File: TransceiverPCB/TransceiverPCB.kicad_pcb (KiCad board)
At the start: 2 copper layers, 1 part, among them U1 XC7A35T-1FTG256C

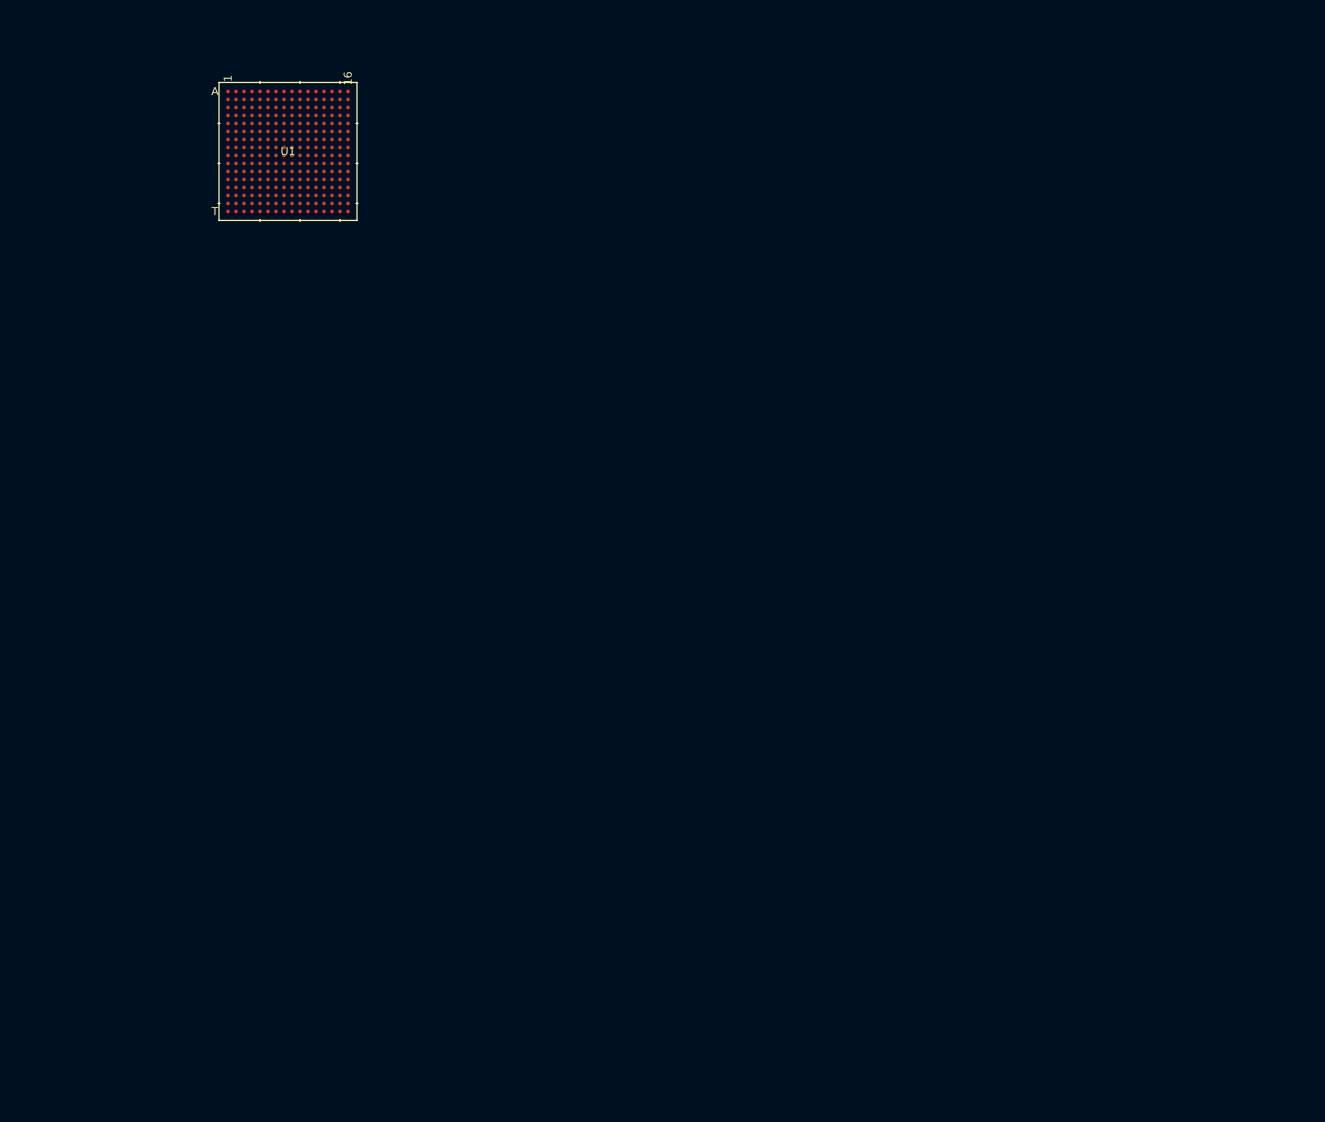
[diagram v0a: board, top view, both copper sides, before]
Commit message: Began PCB
Filled in footprints for components, and began organization of PCB footprints
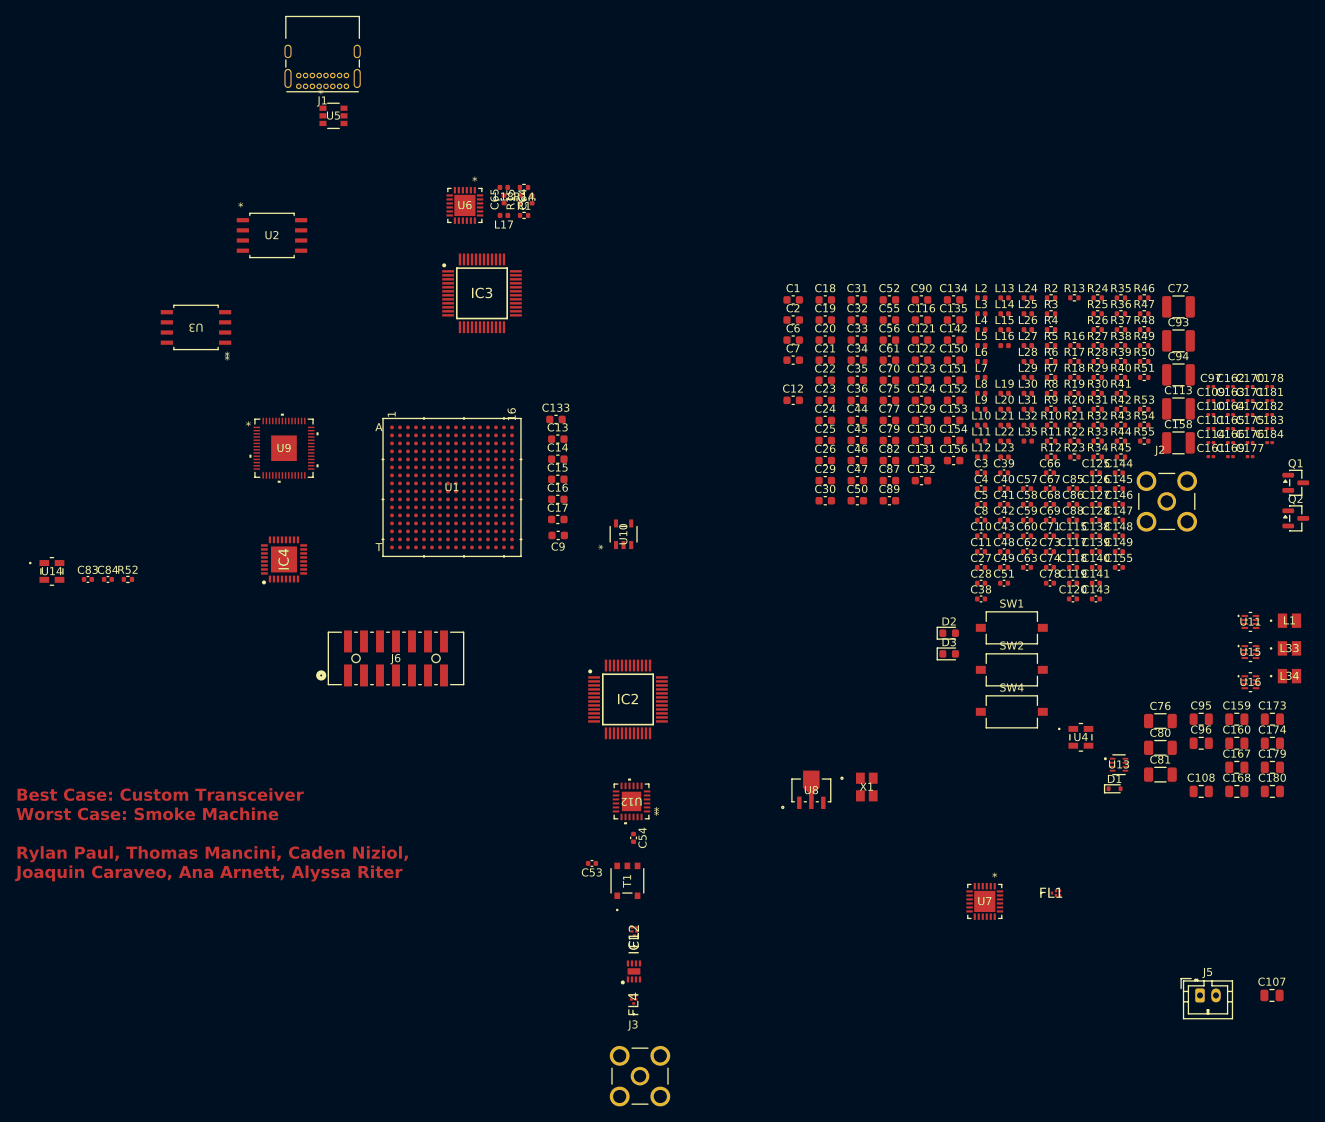
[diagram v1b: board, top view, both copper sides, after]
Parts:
- added C1: 0.1uF, Capacitor_SMD:C_0603_1608Metric, F.Cu at (130.2, 62.6)
- added C10: 22pF, Capacitor_SMD:C_0402_1005Metric, F.Cu at (153.6, 92.1)
- added C107: 4.7uF, Capacitor_SMD:C_0805_2012Metric, F.Cu at (190.0, 149.5)
- added C108: 4.7uF, Capacitor_SMD:C_0805_2012Metric, F.Cu at (181.2, 124.0)
- added C109: 0.47uF, Capacitor_SMD:C_0201_0603Metric, F.Cu at (182.4, 75.2)
- added C11: 22pF, Capacitor_SMD:C_0402_1005Metric, F.Cu at (153.6, 94.0)
- added C110: 0.47uF, Capacitor_SMD:C_0201_0603Metric, F.Cu at (182.4, 76.9)
- added C111: 0.47uF, Capacitor_SMD:C_0201_0603Metric, F.Cu at (182.4, 78.7)
- added C113: 47uF, Capacitor_SMD:C_1210_3225Metric, F.Cu at (178.3, 76.2)
- added C114: 0.47uF, Capacitor_SMD:C_0201_0603Metric, F.Cu at (182.4, 80.4)
- added C115: 120pF, Capacitor_SMD:C_0402_1005Metric, F.Cu at (165.1, 92.1)
- added C116: 0.1uF, Capacitor_SMD:C_0603_1608Metric, F.Cu at (146.2, 65.1)
- added C117: 120pF, Capacitor_SMD:C_0402_1005Metric, F.Cu at (165.1, 94.0)
- added C118: 3.3pF, Capacitor_SMD:C_0402_1005Metric, F.Cu at (165.1, 96.0)
- added C119: 4.7pF, Capacitor_SMD:C_0402_1005Metric, F.Cu at (165.1, 98.0)
- added C12: 10uF, Capacitor_SMD:C_0603_1608Metric, F.Cu at (130.2, 75.1)
- added C120: 3.3pF, Capacitor_SMD:C_0402_1005Metric, F.Cu at (165.1, 99.9)
- added C121: 0.1uF, Capacitor_SMD:C_0603_1608Metric, F.Cu at (146.2, 67.6)
- added C122: 0.1uF, Capacitor_SMD:C_0603_1608Metric, F.Cu at (146.2, 70.1)
- added C123: 0.1uF, Capacitor_SMD:C_0603_1608Metric, F.Cu at (146.2, 72.6)
- added C124: 3.3pF, Capacitor_SMD:C_0603_1608Metric, F.Cu at (146.2, 75.1)
- added C125: 4.7pF, Capacitor_SMD:C_0402_1005Metric, F.Cu at (168.0, 84.2)
- added C126: 3.3pF, Capacitor_SMD:C_0402_1005Metric, F.Cu at (168.0, 86.2)
- added C127: 1nF, Capacitor_SMD:C_0402_1005Metric, F.Cu at (168.0, 88.1)
- added C128: 1nF, Capacitor_SMD:C_0402_1005Metric, F.Cu at (168.0, 90.1)
- added C129: 0.1uF, Capacitor_SMD:C_0603_1608Metric, F.Cu at (146.2, 77.6)
- added C13: 1uF, Capacitor_SMD:C_0603_1608Metric, F.Cu at (100.7, 80.0)
- added C130: 0.1uF, Capacitor_SMD:C_0603_1608Metric, F.Cu at (146.2, 80.1)
- added C131: 0.1uF, Capacitor_SMD:C_0603_1608Metric, F.Cu at (146.2, 82.6)
- added C132: 0.1uF, Capacitor_SMD:C_0603_1608Metric, F.Cu at (146.2, 85.2)
- added C133: 0.1uF, Capacitor_SMD:C_0603_1608Metric, F.Cu at (100.5, 77.5)
- added C134: 0.1uF, Capacitor_SMD:C_0603_1608Metric, F.Cu at (150.2, 62.6)
- added C135: 0.1uF, Capacitor_SMD:C_0603_1608Metric, F.Cu at (150.2, 65.1)
- added C138: 2700pF, Capacitor_SMD:C_0402_1005Metric, F.Cu at (168.0, 92.1)
- added C139: 39nF, Capacitor_SMD:C_0402_1005Metric, F.Cu at (168.0, 94.0)
- added C14: 100nF, Capacitor_SMD:C_0603_1608Metric, F.Cu at (100.7, 82.5)
- added C140: 1200pF, Capacitor_SMD:C_0402_1005Metric, F.Cu at (168.0, 96.0)
- added C141: 120pF, Capacitor_SMD:C_0402_1005Metric, F.Cu at (168.0, 98.0)
- added C142: 0.1uF, Capacitor_SMD:C_0603_1608Metric, F.Cu at (150.2, 67.6)
- added C143: 3.3pF, Capacitor_SMD:C_0402_1005Metric, F.Cu at (168.0, 99.9)
- added C144: 3.3pF, Capacitor_SMD:C_0402_1005Metric, F.Cu at (170.9, 84.2)
- added C145: 120pF, Capacitor_SMD:C_0402_1005Metric, F.Cu at (170.9, 86.2)
- added C146: 4.7pF, Capacitor_SMD:C_0402_1005Metric, F.Cu at (170.9, 88.1)
- added C147: 4.7pF, Capacitor_SMD:C_0402_1005Metric, F.Cu at (170.9, 90.1)
- added C148: 3.3pF, Capacitor_SMD:C_0402_1005Metric, F.Cu at (170.9, 92.1)
- added C149: 3.3pF, Capacitor_SMD:C_0402_1005Metric, F.Cu at (170.9, 94.0)
- added C15: 100nF, Capacitor_SMD:C_0603_1608Metric, F.Cu at (100.7, 85.0)
- added C150: 1nF, Capacitor_SMD:C_0603_1608Metric, F.Cu at (150.2, 70.1)
- added C151: 1nF, Capacitor_SMD:C_0603_1608Metric, F.Cu at (150.2, 72.6)
- added C152: 0.1uF, Capacitor_SMD:C_0603_1608Metric, F.Cu at (150.2, 75.1)
- added C153: .1uF, Capacitor_SMD:C_0603_1608Metric, F.Cu at (150.2, 77.6)
- added C154: .1uF, Capacitor_SMD:C_0603_1608Metric, F.Cu at (150.2, 80.1)
- added C155: 10pF, Capacitor_SMD:C_0402_1005Metric, F.Cu at (170.9, 96.0)
- added C156: 0.1uF, Capacitor_SMD:C_0603_1608Metric, F.Cu at (150.2, 82.6)
- added C158: 47uF, Capacitor_SMD:C_1210_3225Metric, F.Cu at (178.3, 80.4)
- added C159: 4.7uF, Capacitor_SMD:C_0805_2012Metric, F.Cu at (185.6, 115.0)
- added C16: 100nF, Capacitor_SMD:C_0603_1608Metric, F.Cu at (100.7, 87.5)
- added C160: 4.7uF, Capacitor_SMD:C_0805_2012Metric, F.Cu at (185.6, 118.0)
- added C161: 0.47uF, Capacitor_SMD:C_0201_0603Metric, F.Cu at (182.4, 82.2)
- added C162: 0.47uF, Capacitor_SMD:C_0201_0603Metric, F.Cu at (184.8, 73.4)
- added C163: 0.47uF, Capacitor_SMD:C_0201_0603Metric, F.Cu at (184.8, 75.2)
- added C164: 0.47uF, Capacitor_SMD:C_0201_0603Metric, F.Cu at (184.8, 76.9)
- added C165: 0.47uF, Capacitor_SMD:C_0201_0603Metric, F.Cu at (184.8, 78.7)
- added C166: 0.47uF, Capacitor_SMD:C_0201_0603Metric, F.Cu at (184.8, 80.4)
- added C167: 4.7uF, Capacitor_SMD:C_0805_2012Metric, F.Cu at (185.6, 121.0)
- added C168: 4.7uF, Capacitor_SMD:C_0805_2012Metric, F.Cu at (185.6, 124.0)
- added C169: 0.47uF, Capacitor_SMD:C_0201_0603Metric, F.Cu at (184.8, 82.2)
- added C17: 100nF, Capacitor_SMD:C_0603_1608Metric, F.Cu at (100.7, 90.0)
- added C170: 0.47uF, Capacitor_SMD:C_0201_0603Metric, F.Cu at (187.3, 73.4)
- added C171: 0.47uF, Capacitor_SMD:C_0201_0603Metric, F.Cu at (187.3, 75.2)
- added C172: 0.47uF, Capacitor_SMD:C_0201_0603Metric, F.Cu at (187.3, 76.9)
- added C173: 4.7uF, Capacitor_SMD:C_0805_2012Metric, F.Cu at (190.1, 115.0)
- added C174: 4.7uF, Capacitor_SMD:C_0805_2012Metric, F.Cu at (190.1, 118.0)
- added C175: 0.47uF, Capacitor_SMD:C_0201_0603Metric, F.Cu at (187.3, 78.7)
- added C176: 0.47uF, Capacitor_SMD:C_0201_0603Metric, F.Cu at (187.3, 80.4)
- added C177: 0.47uF, Capacitor_SMD:C_0201_0603Metric, F.Cu at (187.3, 82.2)
- added C178: 0.47uF, Capacitor_SMD:C_0201_0603Metric, F.Cu at (189.7, 73.4)
- added C179: 4.7uF, Capacitor_SMD:C_0805_2012Metric, F.Cu at (190.1, 121.0)
- added C18: 100nF, Capacitor_SMD:C_0603_1608Metric, F.Cu at (134.2, 62.6)
- added C180: 4.7uF, Capacitor_SMD:C_0805_2012Metric, F.Cu at (190.1, 124.0)
- added C181: 0.47uF, Capacitor_SMD:C_0201_0603Metric, F.Cu at (189.7, 75.2)
- added C182: 0.47uF, Capacitor_SMD:C_0201_0603Metric, F.Cu at (189.7, 76.9)
- added C183: 0.47uF, Capacitor_SMD:C_0201_0603Metric, F.Cu at (189.7, 78.7)
- added C184: 0.47uF, Capacitor_SMD:C_0201_0603Metric, F.Cu at (189.7, 80.4)
- added C19: 100nF, Capacitor_SMD:C_0603_1608Metric, F.Cu at (134.2, 65.1)
- added C2: 0.1uF, Capacitor_SMD:C_0603_1608Metric, F.Cu at (130.2, 65.1)
- added C20: 100nF, Capacitor_SMD:C_0603_1608Metric, F.Cu at (134.2, 67.6)
- added C21: 1uF, Capacitor_SMD:C_0603_1608Metric, F.Cu at (134.2, 70.1)
- added C22: 100nF, Capacitor_SMD:C_0603_1608Metric, F.Cu at (134.2, 72.6)
- added C23: 100nF, Capacitor_SMD:C_0603_1608Metric, F.Cu at (134.2, 75.1)
- added C24: 1uF, Capacitor_SMD:C_0603_1608Metric, F.Cu at (134.2, 77.6)
- added C25: 1uF, Capacitor_SMD:C_0603_1608Metric, F.Cu at (134.2, 80.1)
- added C26: 0.1uF, Capacitor_SMD:C_0603_1608Metric, F.Cu at (134.2, 82.6)
- added C27: 4.7uF, Capacitor_SMD:C_0402_1005Metric, F.Cu at (153.6, 96.0)
- added C28: 0.1uF, Capacitor_SMD:C_0402_1005Metric, F.Cu at (153.6, 98.0)
- added C29: 10uF, Capacitor_SMD:C_0603_1608Metric, F.Cu at (134.2, 85.2)
- added C3: 22nF, Capacitor_SMD:C_0402_1005Metric, F.Cu at (153.6, 84.2)
- added C30: 100nF, Capacitor_SMD:C_0603_1608Metric, F.Cu at (134.2, 87.7)
- added C31: 10uF, Capacitor_SMD:C_0603_1608Metric, F.Cu at (138.2, 62.6)
- added C32: 10uF, Capacitor_SMD:C_0603_1608Metric, F.Cu at (138.2, 65.1)
- added C33: 10uF, Capacitor_SMD:C_0603_1608Metric, F.Cu at (138.2, 67.6)
- added C34: 10uF, Capacitor_SMD:C_0603_1608Metric, F.Cu at (138.2, 70.1)
- added C35: 100nF, Capacitor_SMD:C_0603_1608Metric, F.Cu at (138.2, 72.6)
- added C36: 1uF, Capacitor_SMD:C_0603_1608Metric, F.Cu at (138.2, 75.1)
- added C38: 270pF, Capacitor_SMD:C_0402_1005Metric, F.Cu at (153.6, 99.9)
- added C39: 270pF, Capacitor_SMD:C_0402_1005Metric, F.Cu at (156.5, 84.2)
- added C4: 22nF, Capacitor_SMD:C_0402_1005Metric, F.Cu at (153.6, 86.2)
- added C40: 91pF, Capacitor_SMD:C_0402_1005Metric, F.Cu at (156.5, 86.2)
- added C41: 91pF, Capacitor_SMD:C_0402_1005Metric, F.Cu at (156.5, 88.1)
- added C42: 68pF, Capacitor_SMD:C_0402_1005Metric, F.Cu at (156.5, 90.1)
- added C43: 68pF, Capacitor_SMD:C_0402_1005Metric, F.Cu at (156.5, 92.1)
- added C44: 1uF, Capacitor_SMD:C_0603_1608Metric, F.Cu at (138.2, 77.6)
- added C45: 1uF, Capacitor_SMD:C_0603_1608Metric, F.Cu at (138.2, 80.1)
- added C46: .1uF, Capacitor_SMD:C_0603_1608Metric, F.Cu at (138.2, 82.6)
- added C47: .1uF, Capacitor_SMD:C_0603_1608Metric, F.Cu at (138.2, 85.2)
- added C48: 100pF, Capacitor_SMD:C_0402_1005Metric, F.Cu at (156.5, 94.0)
- added C49: 100pF, Capacitor_SMD:C_0402_1005Metric, F.Cu at (156.5, 96.0)
- added C5: 100pF, Capacitor_SMD:C_0402_1005Metric, F.Cu at (153.6, 88.1)
- added C50: .1uF, Capacitor_SMD:C_0603_1608Metric, F.Cu at (138.2, 87.7)
- added C51: 100pF, Capacitor_SMD:C_0402_1005Metric, F.Cu at (156.5, 98.0)
- added C52: .1uF, Capacitor_SMD:C_0603_1608Metric, F.Cu at (142.2, 62.6)
- added C53: 1000pF, Capacitor_SMD:C_0402_1005Metric, F.Cu at (105.0, 133.0)
- added C54: 1000pF, Capacitor_SMD:C_0402_1005Metric, F.Cu at (110.2, 129.8)
- added C55: 1uF, Capacitor_SMD:C_0603_1608Metric, F.Cu at (142.2, 65.1)
- added C56: 1uF, Capacitor_SMD:C_0603_1608Metric, F.Cu at (142.2, 67.6)
- added C57: 47pF, Capacitor_SMD:C_0402_1005Metric, F.Cu at (159.4, 86.2)
- added C58: 6.8pF, Capacitor_SMD:C_0402_1005Metric, F.Cu at (159.4, 88.1)
- added C59: 100pF, Capacitor_SMD:C_0402_1005Metric, F.Cu at (159.4, 90.1)
- added C6: 0.1uF, Capacitor_SMD:C_0603_1608Metric, F.Cu at (130.2, 67.6)
- added C60: 10nF, Capacitor_SMD:C_0402_1005Metric, F.Cu at (159.4, 92.1)
- added C61: 10uF, Capacitor_SMD:C_0603_1608Metric, F.Cu at (142.2, 70.1)
- added C62: 47pF, Capacitor_SMD:C_0402_1005Metric, F.Cu at (159.4, 94.0)
- added C63: 2.2pF, Capacitor_SMD:C_0402_1005Metric, F.Cu at (159.4, 96.0)
- added C64: 53.62pF, Capacitor_SMD:C_0402_1005Metric, F.Cu at (97.5, 50.0)
- added C65: 350.1pF, Capacitor_SMD:C_0402_1005Metric, F.Cu at (94.0, 50.0)
- added C66: 53.62pF, Capacitor_SMD:C_0402_1005Metric, F.Cu at (162.2, 84.2)
- added C67: 350.1pF, Capacitor_SMD:C_0402_1005Metric, F.Cu at (162.2, 86.2)
- added C68: 10uF, Capacitor_SMD:C_0402_1005Metric, F.Cu at (162.2, 88.1)
- added C69: 4.7uF, Capacitor_SMD:C_0402_1005Metric, F.Cu at (162.2, 90.1)
- added C7: 0.1uF, Capacitor_SMD:C_0603_1608Metric, F.Cu at (130.2, 70.1)
- added C70: 100nF, Capacitor_SMD:C_0603_1608Metric, F.Cu at (142.2, 72.6)
- added C71: 10uF, Capacitor_SMD:C_0402_1005Metric, F.Cu at (162.2, 92.1)
- added C72: 47uF, Capacitor_SMD:C_1210_3225Metric, F.Cu at (178.3, 63.4)
- added C73: 4.7uF, Capacitor_SMD:C_0402_1005Metric, F.Cu at (162.2, 94.0)
- added C74: 10uF, Capacitor_SMD:C_0402_1005Metric, F.Cu at (162.2, 96.0)
- added C75: 0.1uF, Capacitor_SMD:C_0603_1608Metric, F.Cu at (142.2, 75.1)
- added C76: 47uF, Capacitor_SMD:C_1206_3216Metric, F.Cu at (176.1, 115.2)
- added C77: 0.1uF, Capacitor_SMD:C_0603_1608Metric, F.Cu at (142.2, 77.6)
- added C78: 6.8nF, Capacitor_SMD:C_0402_1005Metric, F.Cu at (162.2, 98.0)
- added C79: 100nF, Capacitor_SMD:C_0603_1608Metric, F.Cu at (142.2, 80.1)
- added C8: 100pF, Capacitor_SMD:C_0402_1005Metric, F.Cu at (153.6, 90.1)
- added C80: 22uF, Capacitor_SMD:C_1206_3216Metric, F.Cu at (176.1, 118.5)
- added C81: 22uF, Capacitor_SMD:C_1206_3216Metric, F.Cu at (176.1, 121.9)
- added C82: 0.1uF, Capacitor_SMD:C_0603_1608Metric, F.Cu at (142.2, 82.6)
- added C83: 1nF, Capacitor_SMD:C_0402_1005Metric, F.Cu at (42.0, 97.5)
- added C84: 1nF, Capacitor_SMD:C_0402_1005Metric, F.Cu at (44.5, 97.5)
- added C85: 22pF, Capacitor_SMD:C_0402_1005Metric, F.Cu at (165.1, 86.2)
- added C86: 10pF, Capacitor_SMD:C_0402_1005Metric, F.Cu at (165.1, 88.1)
- added C87: 0.1uF, Capacitor_SMD:C_0603_1608Metric, F.Cu at (142.2, 85.2)
- added C88: 10pF, Capacitor_SMD:C_0402_1005Metric, F.Cu at (165.1, 90.1)
- added C89: 0.1uF, Capacitor_SMD:C_0603_1608Metric, F.Cu at (142.2, 87.7)
- added C9: 100nF, Capacitor_SMD:C_0603_1608Metric, F.Cu at (100.8, 92.0)
- added C90: 1uF, Capacitor_SMD:C_0603_1608Metric, F.Cu at (146.2, 62.6)
- added C93: 100uF, Capacitor_SMD:C_1210_3225Metric, F.Cu at (178.3, 67.7)
- added C94: 100uF, Capacitor_SMD:C_1210_3225Metric, F.Cu at (178.3, 71.9)
- added C95: 4.7uF, Capacitor_SMD:C_0805_2012Metric, F.Cu at (181.2, 115.0)
- added C96: 4.7uF, Capacitor_SMD:C_0805_2012Metric, F.Cu at (181.2, 118.0)
- added C97: 0.47uF, Capacitor_SMD:C_0201_0603Metric, F.Cu at (182.4, 73.4)
- added D1: ESD5Z5V0, LIB_IRISHSAT:P38_SOD-523, F.Cu at (169.6, 123.7)
- added D2: LED, LED_SMD:LED_0603_1608Metric, F.Cu at (149.6, 104.2)
- added D3: LED, LED_SMD:LED_0603_1608Metric, F.Cu at (149.6, 106.8)
- added FL1: B39921B2672P810, LIB_IRISHSAT:B39921B2672P810, F.Cu at (163.0, 136.7)
- added FL2: B39921B2672P810, LIB_IRISHSAT:B39921B2672P810, F.Cu at (110.3, 141.5)
- added FL4: B39921B2672P810, LIB_IRISHSAT:B39921B2672P810, F.Cu at (110.2, 150.0)
- added IC1: QPL6220QTR7, LIB_IRISHSAT:SON50P200X200X90-9N-D, F.Cu at (110.2, 146.5)
- added IC2: AD9218BSTZ-65, LIB_IRISHSAT:QFP50P900X900X160-48N, F.Cu at (109.5, 112.5)
- added IC3: AD9763ASTZ, LIB_IRISHSAT:QFP50P900X900X160-48N, F.Cu at (91.2, 61.7)
- added IC4: ADF4351BCPZ-RL7, LIB_IRISHSAT:QFN50P500X500X80-33N-D, F.Cu at (66.5, 95.0)
- added J1: USB4085-GF-A_REVB, Connector_USB:USB_C_Receptacle_GCT_USB4085, F.Cu at (74.3, 35.9)
- added J2: RFPC-SMA27-F, LIB_IRISHSAT:GRADCONN_RFPC-SMA27-F, F.Cu at (176.8, 87.8)
- added J3: RFPC-SMA27-F, LIB_IRISHSAT:GRADCONN_RFPC-SMA27-F, F.Cu at (111.0, 159.6)
- added J5: Conn_01x02, Connector_JST:JST_PH_B2B-PH-K_1x02_P2.00mm_Vertical, F.Cu at (181.0, 149.5)
- added J6: 878321420, LIB_IRISHSAT:CONN14_878321420_MOL, F.Cu at (80.5, 107.4)
- added L1: 2.2uH, LIB_IRISHSAT:IND_DFE2016_MUR, F.Cu at (192.2, 102.7)
- added L10: 27uH, Inductor_SMD:L_0402_1005Metric, F.Cu at (153.7, 78.2)
- added L11: 10uH, Inductor_SMD:L_0402_1005Metric, F.Cu at (153.7, 80.2)
- added L12: 10uH, Inductor_SMD:L_0402_1005Metric, F.Cu at (153.7, 82.2)
- added L13: 27uH, Inductor_SMD:L_0402_1005Metric, F.Cu at (156.6, 62.3)
- added L14: 10uH, Inductor_SMD:L_0402_1005Metric, F.Cu at (156.6, 64.3)
- added L15: 10uH, Inductor_SMD:L_0402_1005Metric, F.Cu at (156.6, 66.3)
- added L16: 47nH, Inductor_SMD:L_0402_1005Metric, F.Cu at (156.6, 68.3)
- added L17: 771.1nH, Inductor_SMD:L_0402_1005Metric, F.Cu at (94.0, 52.0)
- added L18: 771.1nH, Inductor_SMD:L_0402_1005Metric, F.Cu at (94.0, 48.5)
- added L19: 771.1nH, Inductor_SMD:L_0402_1005Metric, F.Cu at (156.6, 74.2)
- added L2: 120nH, Inductor_SMD:L_0402_1005Metric, F.Cu at (153.7, 62.3)
- added L20: 771.1nH, Inductor_SMD:L_0402_1005Metric, F.Cu at (156.6, 76.2)
- added L21: 2.7nH, Inductor_SMD:L_0402_1005Metric, F.Cu at (156.6, 78.2)
- added L22: 2.7nH, Inductor_SMD:L_0402_1005Metric, F.Cu at (156.6, 80.2)
- added L23: 2.7nH, Inductor_SMD:L_0402_1005Metric, F.Cu at (156.6, 82.2)
- added L24: 2.7nH, Inductor_SMD:L_0402_1005Metric, F.Cu at (159.5, 62.3)
- added L25: 19nH, Inductor_SMD:L_0402_1005Metric, F.Cu at (159.5, 64.3)
- added L26: 19nH, Inductor_SMD:L_0402_1005Metric, F.Cu at (159.5, 66.3)
- added L27: 19nH, Inductor_SMD:L_0402_1005Metric, F.Cu at (159.5, 68.3)
- added L28: 19nH, Inductor_SMD:L_0402_1005Metric, F.Cu at (159.5, 70.3)
- added L29: 2.7nH, Inductor_SMD:L_0402_1005Metric, F.Cu at (159.5, 72.2)
- added L3: 120nH, Inductor_SMD:L_0402_1005Metric, F.Cu at (153.7, 64.3)
- added L30: 2.7nH, Inductor_SMD:L_0402_1005Metric, F.Cu at (159.5, 74.2)
- added L31: 2.7nH, Inductor_SMD:L_0402_1005Metric, F.Cu at (159.5, 76.2)
- added L32: 2.7nH, Inductor_SMD:L_0402_1005Metric, F.Cu at (159.5, 78.2)
- added L33: 2.2uH, LIB_IRISHSAT:IND_DFE2016_MUR, F.Cu at (192.2, 106.1)
- added L34: 2.2uH, LIB_IRISHSAT:IND_DFE2016_MUR, F.Cu at (192.2, 109.6)
- added L35: 2.7uH, Inductor_SMD:L_0402_1005Metric, F.Cu at (159.5, 80.2)
- added L4: 27uH, Inductor_SMD:L_0402_1005Metric, F.Cu at (153.7, 66.3)
- added L5: 27uH, Inductor_SMD:L_0402_1005Metric, F.Cu at (153.7, 68.3)
- added L6: 27uH, Inductor_SMD:L_0402_1005Metric, F.Cu at (153.7, 70.3)
- added L7: 27uH, Inductor_SMD:L_0402_1005Metric, F.Cu at (153.7, 72.2)
- added L8: 27uH, Inductor_SMD:L_0402_1005Metric, F.Cu at (153.7, 74.2)
- added L9: 27uH, Inductor_SMD:L_0402_1005Metric, F.Cu at (153.7, 76.2)
- added Q1: AO3401A, Package_TO_SOT_SMD:SOT-23, F.Cu at (193.0, 85.4)
- added Q2: AO3401A, Package_TO_SOT_SMD:SOT-23, F.Cu at (193.0, 89.9)
- added R1: 50, Resistor_SMD:R_0402_1005Metric, F.Cu at (96.5, 52.0)
- added R10: 10k, Resistor_SMD:R_0402_1005Metric, F.Cu at (162.4, 78.2)
- added R11: 500, Resistor_SMD:R_0402_1005Metric, F.Cu at (162.4, 80.2)
- added R12: 500, Resistor_SMD:R_0402_1005Metric, F.Cu at (162.4, 82.2)
- added R13: 1k, Resistor_SMD:R_0402_1005Metric, F.Cu at (165.3, 62.3)
- added R14: 50, Resistor_SMD:R_0402_1005Metric, F.Cu at (96.5, 48.5)
- added R15: 100, Resistor_SMD:R_0402_1005Metric, F.Cu at (96.0, 50.0)
- added R16: 50, Resistor_SMD:R_0402_1005Metric, F.Cu at (165.3, 68.3)
- added R17: 50, Resistor_SMD:R_0402_1005Metric, F.Cu at (165.3, 70.3)
- added R18: 100, Resistor_SMD:R_0402_1005Metric, F.Cu at (165.3, 72.2)
- added R19: 10k, Resistor_SMD:R_0402_1005Metric, F.Cu at (165.3, 74.2)
- added R2: DNF, Resistor_SMD:R_0402_1005Metric, F.Cu at (162.4, 62.3)
- added R20: 1k, Resistor_SMD:R_0402_1005Metric, F.Cu at (165.3, 76.2)
- added R21: 1k, Resistor_SMD:R_0402_1005Metric, F.Cu at (165.3, 78.2)
- added R22: 1k, Resistor_SMD:R_0402_1005Metric, F.Cu at (165.3, 80.2)
- added R23: 1k, Resistor_SMD:R_0402_1005Metric, F.Cu at (165.3, 82.2)
- added R24: 1k, Resistor_SMD:R_0402_1005Metric, F.Cu at (168.2, 62.3)
- added R25: 1k, Resistor_SMD:R_0402_1005Metric, F.Cu at (168.2, 64.3)
- added R26: 1k, Resistor_SMD:R_0402_1005Metric, F.Cu at (168.2, 66.3)
- added R27: 10k, Resistor_SMD:R_0402_1005Metric, F.Cu at (168.2, 68.3)
- added R28: 10k, Resistor_SMD:R_0402_1005Metric, F.Cu at (168.2, 70.3)
- added R29: 1k, Resistor_SMD:R_0402_1005Metric, F.Cu at (168.2, 72.2)
- added R3: 1k, Resistor_SMD:R_0402_1005Metric, F.Cu at (162.4, 64.3)
- added R30: DNF, Resistor_SMD:R_0402_1005Metric, F.Cu at (168.2, 74.2)
- added R31: 470k, Resistor_SMD:R_0402_1005Metric, F.Cu at (168.2, 76.2)
- added R32: 54k, Resistor_SMD:R_0402_1005Metric, F.Cu at (168.2, 78.2)
- added R33: 100, Resistor_SMD:R_0402_1005Metric, F.Cu at (168.2, 80.2)
- added R34: 10k, Resistor_SMD:R_0402_1005Metric, F.Cu at (168.2, 82.2)
- added R35: 360, Resistor_SMD:R_0402_1005Metric, F.Cu at (171.1, 62.3)
- added R36: 680, Resistor_SMD:R_0402_1005Metric, F.Cu at (171.1, 64.3)
- added R37: 100, Resistor_SMD:R_0402_1005Metric, F.Cu at (171.1, 66.3)
- added R38: 10k, Resistor_SMD:R_0402_1005Metric, F.Cu at (171.1, 68.3)
- added R39: 3.32k, Resistor_SMD:R_0402_1005Metric, F.Cu at (171.1, 70.3)
- added R4: 10k, Resistor_SMD:R_0402_1005Metric, F.Cu at (162.4, 66.3)
- added R40: 10k, Resistor_SMD:R_0402_1005Metric, F.Cu at (171.1, 72.2)
- added R41: 10k, Resistor_SMD:R_0402_1005Metric, F.Cu at (171.1, 74.2)
- added R42: 256, Resistor_SMD:R_0402_1005Metric, F.Cu at (171.1, 76.2)
- added R43: 256, Resistor_SMD:R_0402_1005Metric, F.Cu at (171.1, 78.2)
- added R44: 2k, Resistor_SMD:R_0402_1005Metric, F.Cu at (171.1, 80.2)
- added R45: 33, Resistor_SMD:R_0402_1005Metric, F.Cu at (171.1, 82.2)
- added R46: 33, Resistor_SMD:R_0402_1005Metric, F.Cu at (174.0, 62.3)
- added R47: 33, Resistor_SMD:R_0402_1005Metric, F.Cu at (174.0, 64.3)
- added R48: 52.3k, Resistor_SMD:R_0402_1005Metric, F.Cu at (174.0, 66.3)
- added R49: 4.32k, Resistor_SMD:R_0402_1005Metric, F.Cu at (174.0, 68.3)
- added R5: 1k, Resistor_SMD:R_0402_1005Metric, F.Cu at (162.4, 68.3)
- added R50: 127.758k, Resistor_SMD:R_0402_1005Metric, F.Cu at (174.0, 70.3)
- added R51: 28.212k, Resistor_SMD:R_0402_1005Metric, F.Cu at (174.0, 72.2)
- added R52: 51, Resistor_SMD:R_0402_1005Metric, F.Cu at (47.0, 97.5)
- added R53: 10k, Resistor_SMD:R_0402_1005Metric, F.Cu at (174.0, 76.2)
- added R54: 4.7k, Resistor_SMD:R_0402_1005Metric, F.Cu at (174.0, 78.2)
- added R55: 5.1k, Resistor_SMD:R_0402_1005Metric, F.Cu at (174.0, 80.2)
- added R6: 5.1k, Resistor_SMD:R_0402_1005Metric, F.Cu at (162.4, 70.3)
- added R7: 5.1k, Resistor_SMD:R_0402_1005Metric, F.Cu at (162.4, 72.2)
- added R8: 27.4k, Resistor_SMD:R_0402_1005Metric, F.Cu at (162.4, 74.2)
- added R9: 27.4k, Resistor_SMD:R_0402_1005Metric, F.Cu at (162.4, 76.2)
- added SW1: SW_Push, Button_Switch_SMD:SW_Tactile_SPST_NO_Straight_CK_PTS636Sx25SMTRLFS, F.Cu at (157.5, 103.5)
- added SW2: SW_Push, Button_Switch_SMD:SW_Tactile_SPST_NO_Straight_CK_PTS636Sx25SMTRLFS, F.Cu at (157.5, 108.8)
- added SW4: SW_Push, Button_Switch_SMD:SW_Tactile_SPST_NO_Straight_CK_PTS636Sx25SMTRLFS, F.Cu at (157.5, 114.0)
- added T1: ETC1-1-13TR, LIB_IRISHSAT:ETC1-1-13TR_MCM, F.Cu at (109.4, 135.2)
- added U10: AP2112K-3.3TRG1, LIB_IRISHSAT:SOT_RG1_DIO, F.Cu at (109.0, 91.9)
- added U11: TPS62840DLCR, LIB_IRISHSAT:VSON8_2P1X1P6_TEX, F.Cu at (187.3, 102.8)
- added U12: ADL5387ACPZ-R7, LIB_IRISHSAT:CP-24-14_ADI, F.Cu at (109.9, 125.2)
- added U13: TPS62933FDRLR, LIB_IRISHSAT:SOT5X3-8_DRL_TEX, F.Cu at (170.9, 120.7)
- added U14: DSC1001CI2-100.0000T, LIB_IRISHSAT:CDFN4_3P2X2P5_MCH, F.Cu at (37.5, 96.5)
- added U15: TPS62840DLCR, LIB_IRISHSAT:VSON8_2P1X1P6_TEX, F.Cu at (187.3, 106.6)
- added U16: TPS62841DLCR, LIB_IRISHSAT:VSON8_2P1X1P6_TEX, F.Cu at (187.3, 110.3)
- added U2: W25Q32JVSSIQ, LIB_IRISHSAT:SOIC-8_5P28X5P28_WIN, F.Cu at (65.0, 54.5)
- added U3: W25Q32JVSSIQ, LIB_IRISHSAT:SOIC-8_5P28X5P28_WIN, F.Cu at (55.5, 66.0)
- added U4: DSC1001CI2-100.0000T, LIB_IRISHSAT:CDFN4_3P2X2P5_MCH, F.Cu at (166.1, 117.2)
- added U5: LTC4412ES6-TRMPBF, LIB_IRISHSAT:SOT-6_S_LIT, F.Cu at (72.7, 39.5)
- added U6: ADL5375-05ACPZ-R7, LIB_IRISHSAT:CP_24_7_ADI, F.Cu at (89.1, 50.8)
- added U7: ADA4940-2ACPZ-R7, LIB_IRISHSAT:CP_24_7_ADI, F.Cu at (154.1, 137.7)
- added U8: ADL5320ARKZ-R7, LIB_IRISHSAT:RK_3_ADI, F.Cu at (132.4, 123.9)
- added U9: SC09147, LIB_IRISHSAT:QFN56_7X7_RPI, F.Cu at (66.5, 81.1)
- added X1: ABM8-272-T3, LIB_IRISHSAT:ABM8-272-T3_ABR, F.Cu at (139.3, 123.4)
- moved U1 46.7 mm to (87.5, 86.0)
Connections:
- U1 pad F8: unconnected-(U1B-VCCBATT_0-PadF8) -> +1V8
- U1 pad G7: unconnected-(U1B-GNDADC_0-PadG7) -> GND
- U1 pad G8: unconnected-(U1B-VCCADC_0-PadG8) -> +1V8
- U1 pad H7: unconnected-(U1B-VREFN_0-PadH7) -> GND
- U1 pad H8: unconnected-(U1B-VP_0-PadH8) -> GND
- U1 pad J7: unconnected-(U1B-VN_0-PadJ7) -> GND
- U1 pad J8: unconnected-(U1B-VREFP_0-PadJ8) -> GND
- U1 pad K13: unconnected-(U1B-IO_L5P_T0_D06_14-PadK13) -> /D5A_ADC
- U1 pad K7: unconnected-(U1B-DXN_0-PadK7) -> GND
- U1 pad K8: unconnected-(U1B-DXP_0-PadK8) -> GND
- U1 pad L12: unconnected-(U1B-IO_L6P_T0_FCS_B_14-PadL12) -> /D6A_ADC
- U1 pad L13: unconnected-(U1C-IO_L5N_T0_D07_14-PadL13) -> /D4A_ADC
- U1 pad L14: unconnected-(U1C-IO_L4P_T0_D04_14-PadL14) -> /D2A_ADC
- U1 pad L15: unconnected-(U1C-IO_L3P_T0_DQS_PUDC_B_14-PadL15) -> /D0A_ADC
- U1 pad L9: Net-(U1B-PROGRAM_B_0) -> FPGA_RESET
- U1 pad M10: unconnected-(U1C-M1_0-PadM10) -> GND
- U1 pad M11: unconnected-(U1C-M2_0-PadM11) -> GND
- U1 pad M12: unconnected-(U1C-IO_L6N_T0_D08_VREF_14-PadM12) -> /D7A_ADC
- U1 pad M14: unconnected-(U1C-IO_L4N_T0_D05_14-PadM14) -> /D3A_ADC
- U1 pad M15: unconnected-(U1C-IO_L3N_T0_DQS_EMCCLK_14-PadM15) -> /D1A_ADC
- U1 pad M16: unconnected-(U1C-IO_L7P_T1_D09_14-PadM16) -> /D8A_ADC
- U1 pad M9: unconnected-(U1C-M0_0-PadM9) -> Net-(U1C-M0_0)
- U1 pad N13: unconnected-(U1C-IO_L11P_T1_SRCC_14-PadN13) -> /D3B_ADC
- U1 pad N14: unconnected-(U1C-IO_L12P_T1_MRCC_14-PadN14) -> /D5B_ADC
- U1 pad N16: unconnected-(U1C-IO_L7N_T1_D10_14-PadN16) -> /D9A_ADC_MSB
- U1 pad P13: unconnected-(U1C-IO_L11N_T1_SRCC_14-PadP13) -> /D2B_ADC
- U1 pad P14: unconnected-(U1C-IO_L12N_T1_MRCC_14-PadP14) -> /D4B_ADC
- U1 pad P15: unconnected-(U1C-IO_L8P_T1_D11_14-PadP15) -> /D1B_ADC
- U1 pad P16: unconnected-(U1C-IO_L8N_T1_D12_14-PadP16) -> /D0B_ADC
- U1 pad R15: unconnected-(U1C-IO_L9P_T1_DQS_14-PadR15) -> /D6B_ADC
- U1 pad R16: unconnected-(U1C-IO_L9N_T1_DQS_D13_14-PadR16) -> /D7B_ADC
- U1 pad T10: unconnected-(U1C-IO_L22N_T3_A04_D20_14-PadT10) -> /D9B_ADC_MSB
- U1 pad T9: unconnected-(U1C-IO_L22P_T3_A05_D21_14-PadT9) -> /D8B_ADC
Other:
- board text added: "Best Case: Custom Transceiver Worst Case: Smoke Machine Rylan Paul, Thomas Mancini, Caden Niziol, Joaquin Caraveo, Ana Arnett, Alyssa Riter"

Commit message: Grouped Together the Different Parts
I separated all the capacitors and resistors into the groups with the modules that they belong with
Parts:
- moved IC4 196.1 mm to (258.1, 53.3)
- moved U12 155.3 mm to (262.5, 96.1)
- moved FL2 155.1 mm to (262.7, 112.9)
- moved FL4 155.1 mm to (262.7, 121.4)
- moved T1 155.1 mm to (261.9, 106.5)
- moved C53 155.1 mm to (257.5, 104.4)
- moved C54 155.1 mm to (262.7, 101.2)
- moved IC1 155.1 mm to (262.7, 117.9)
- moved J3 155.1 mm to (263.5, 131.0)
- moved C10 143.6 mm to (18.5, 43.5)
- moved C11 143.6 mm to (18.5, 45.5)
- moved C107 143.2 mm to (57.2, 95.8)
- moved R5 142.4 mm to (21.5, 47.5), turned to 180 degrees
- moved R2 142.2 mm to (21.5, 43.0)
- moved R3 142.2 mm to (21.5, 45.0)
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
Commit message: Began work on pcb layout
usb and battery modules done, need work on power plane and voltage regulators
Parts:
- moved J5 175.8 mm to (60.0, 22.0), turned to 180 degrees
- moved R6 79.3 mm to (105.0, 15.5)
- moved R7 79.3 mm to (105.0, 17.5)
- moved U11 31.0 mm to (68.2, 53.2)
- moved L34 31.0 mm to (63.0, 53.0)
- moved C73 31.0 mm to (58.9, 52.5)
- moved C74 31.0 mm to (58.9, 54.5)
- moved C81 30.9 mm to (77.5, 23.0), turned to -90 degrees
- moved U13 29.7 mm to (69.3, 21.7)
- moved R51 28.2 mm to (64.5, 18.5), turned to 90 degrees
- moved C78 28.0 mm to (69.5, 19.0), turned to -90 degrees
- moved R34 26.0 mm to (75.0, 19.5), turned to 90 degrees
- moved R32 25.1 mm to (75.0, 22.5), turned to -90 degrees
- moved C80 24.1 mm to (75.0, 26.0), turned to 90 degrees
- moved L35 23.5 mm to (73.5, 23.0)
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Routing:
- net +5V: track 0.00 -> 25.5 mm, vias 0 -> 2
- net +USB5V: track 0.00 -> 15.5 mm, vias 0 -> 2
- net Net-(Q2-G): track 0.00 -> 14.5 mm, vias 0 -> 2
- net +BATT: track 0.00 -> 8.51 mm
- net FPGA_JTAG_VREF: track 0.00 -> 8.30 mm, vias 0 -> 1
- net Net-(Q2-D): track 0.00 -> 7.29 mm
- net Net-(U13-FB): track 0.00 -> 6.88 mm
- net Net-(U13-EN): track 0.00 -> 6.18 mm
- net Net-(Q1-G): track 0.00 -> 4.23 mm
- net Net-(U13-SW): track 0.00 -> 3.82 mm
- net GND: track 0.00 -> 3.81 mm, vias 0 -> 25
- net Net-(U13-SS): track 0.00 -> 2.65 mm
- net Net-(U10-EN): track 0.00 -> 1.34 mm
- added copper zone on In2.Cu, net +5V
- added copper zone on In1.Cu, net GND
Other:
- copper layers 2 -> 6

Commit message: done with power
finished power
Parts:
- moved C57 167.0 mm to (149.3, -20.6)
- moved C58 167.0 mm to (149.3, -18.6)
- moved C61 167.0 mm to (156.2, -2.75)
- moved C63 167.0 mm to (166.5, 0.75)
- moved FL1 167.0 mm to (163.0, -10.3)
- moved L16 167.0 mm to (156.0, -5.25)
- moved C59 167.0 mm to (166.5, -5.16)
- moved C60 167.0 mm to (166.5, -3.19)
- moved C62 167.0 mm to (166.5, -1.22)
- moved U8 167.0 mm to (161.2, -1.55)
- moved J3 134.3 mm to (151.1, 57.5), turned to 90 degrees
- moved C141 128.0 mm to (271.1, -47.4)
- moved C142 128.0 mm to (260.8, -56.0)
- moved C143 128.0 mm to (271.1, -45.5)
- moved C144 128.0 mm to (271.1, -58.8)
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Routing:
- net +5V: track 25.5 -> 43.2 mm, vias 2 -> 4
- net +1V: track 0.00 -> 4.80 mm
- net +3V: track 0.00 -> 4.39 mm
- net Net-(U16-VOS): track 0.00 -> 2.14 mm
- net Net-(U15-VOS): track 0.00 -> 2.09 mm
- net Net-(U11-VOS): track 0.00 -> 2.08 mm
- net +1V8: track 0.00 -> 2.07 mm
- net Net-(U15-VSET): track 0.00 -> 1.51 mm
- net Net-(U16-VSET): track 0.00 -> 1.03 mm
- net GND: track 3.81 -> 4.73 mm, vias 25 -> 29

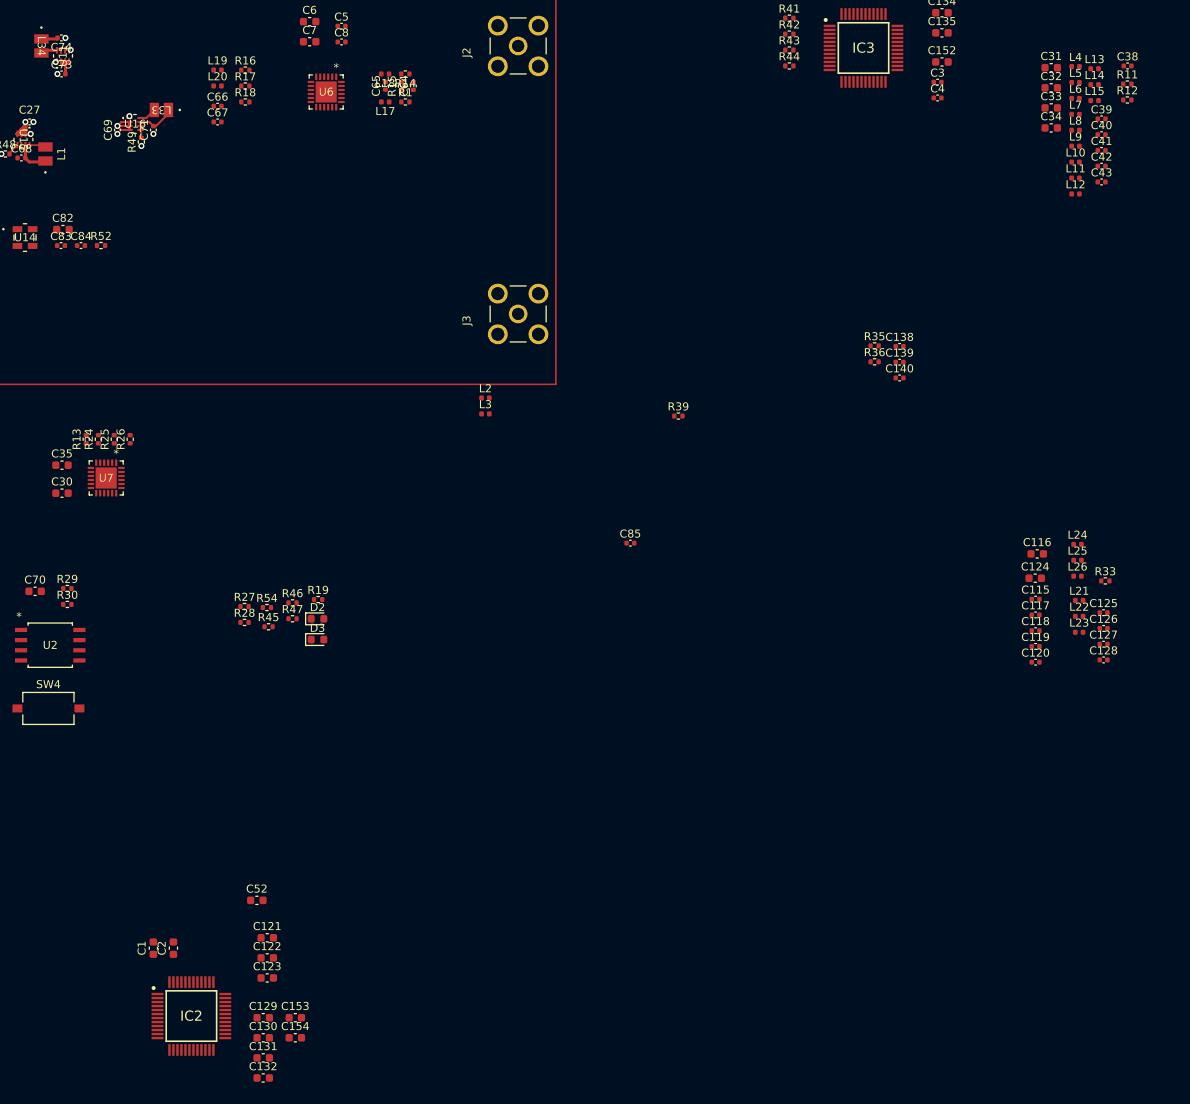
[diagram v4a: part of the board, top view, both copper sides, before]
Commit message: Somewhat routed ADC, LPF, and ADC Driver
-Somewhat routed ADC
-ADC Driver
-Made LPF filter
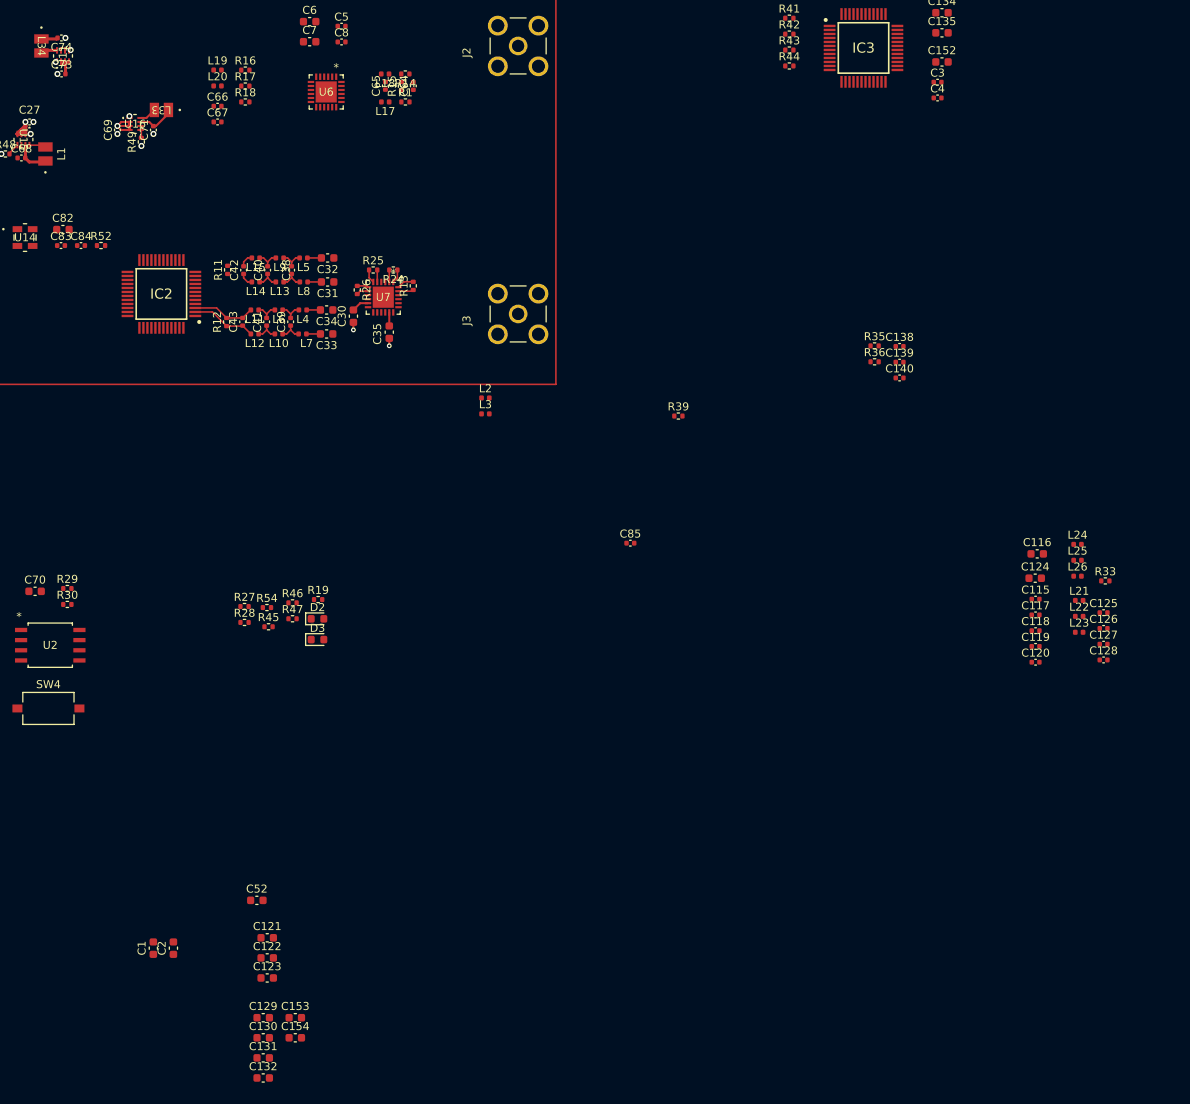
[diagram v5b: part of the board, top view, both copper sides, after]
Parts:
- moved R12 116.0 mm to (114.7, 58.5), turned to 90 degrees
- moved R11 114.8 mm to (114.8, 52.0), turned to 90 degrees
- moved C43 108.8 mm to (116.7, 58.5), turned to 90 degrees
- moved C42 108.0 mm to (116.8, 52.0), turned to 90 degrees
- moved L14 107.7 mm to (118.3, 53.5), turned to 180 degrees
- moved C38 107.6 mm to (122.8, 52.0), turned to 90 degrees
- moved L15 106.7 mm to (118.3, 50.5), turned to 180 degrees
- moved C41 106.5 mm to (119.7, 58.5), turned to 90 degrees
- moved C40 105.6 mm to (119.8, 52.0), turned to 90 degrees
- moved L13 105.3 mm to (121.3, 53.5), turned to 180 degrees
- moved C39 104.5 mm to (122.7, 58.5), turned to 90 degrees
- moved L12 104.1 mm to (118.2, 60.0), turned to 180 degrees
- moved L11 103.9 mm to (118.2, 57.0), turned to 180 degrees
- moved L6 103.0 mm to (121.2, 57.0), turned to 180 degrees
- moved L10 101.9 mm to (121.2, 60.0), turned to 180 degrees
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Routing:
- net /I+ADC_IN: track 0.00 -> 8.14 mm
- net /I-ADC_IN: track 0.00 -> 7.88 mm
- net +1V: track 4.80 -> 8.67 mm
- net Net-(C41-Pad1): track 0.00 -> 2.98 mm
- net Net-(C40-Pad2): track 0.00 -> 2.98 mm
- net Net-(C39-Pad1): track 0.00 -> 2.95 mm
- net Net-(C38-Pad2): track 0.00 -> 2.95 mm
- net Net-(C41-Pad2): track 0.00 -> 2.94 mm
- net Net-(C39-Pad2): track 0.00 -> 2.94 mm
- net Net-(C40-Pad1): track 0.00 -> 2.94 mm
- net Net-(C38-Pad1): track 0.00 -> 2.94 mm
- net /DEMOD_IN1+: track 0.00 -> 2.13 mm
- net Net-(U7-FB1-): track 0.00 -> 1.91 mm
- net GND: track 4.73 -> 6.61 mm, vias 29 -> 31
- net /Q-ADC_IN: track 0.00 -> 1.86 mm
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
